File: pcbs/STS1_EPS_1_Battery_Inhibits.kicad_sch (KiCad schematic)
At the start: 0 parts

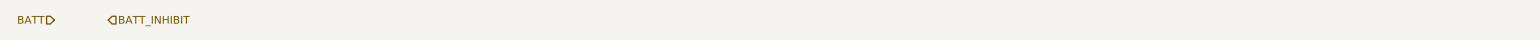
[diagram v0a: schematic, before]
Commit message: Worked on STS_EPS_1.
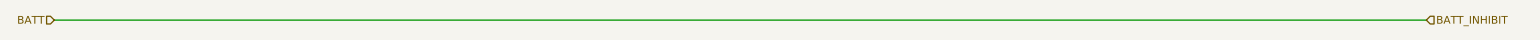
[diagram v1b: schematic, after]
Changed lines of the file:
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@@
 (kicad_sch (version 20211123) (generator eeschema)
   (paper "A4")
+  (wire (pts (xy 25.4 27.94) (xy 251.46 27.94))
+    (stroke (width 0) (type default) (color 0 0 0 0))
+  )
   (hierarchical_label "BATT" (shape input) (at 25.4 27.94 180)
     (effects (font (size 1.27 1.27)) (justify right))
   )
-  (hierarchical_label "BATT_INHIBIT" (shape input) (at 34.29 27.94 0)
+  (hierarchical_label "BATT_INHIBIT" (shape input) (at 251.46 27.94 0)
     (effects (font (size 1.27 1.27)) (justify left))
   )
